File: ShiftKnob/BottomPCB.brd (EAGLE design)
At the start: 38.1 x 38 mm, 38 parts, among them IC2 UA78M05DCY, J1 AVR_SPI_PRG_6PTH, Q1 16MHz, Q2 MOSFET-NCHANNELSMD, Q3 MOSFET-PCHANNELSMD, Q4 MOSFET-NCHANNELSMD, Q5 MOSFET-NCHANNELSMD, Q6 MOSFET-NCHANNELSMD, U1 ATMEGA328, U3 FT232RL-BASICSSOP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

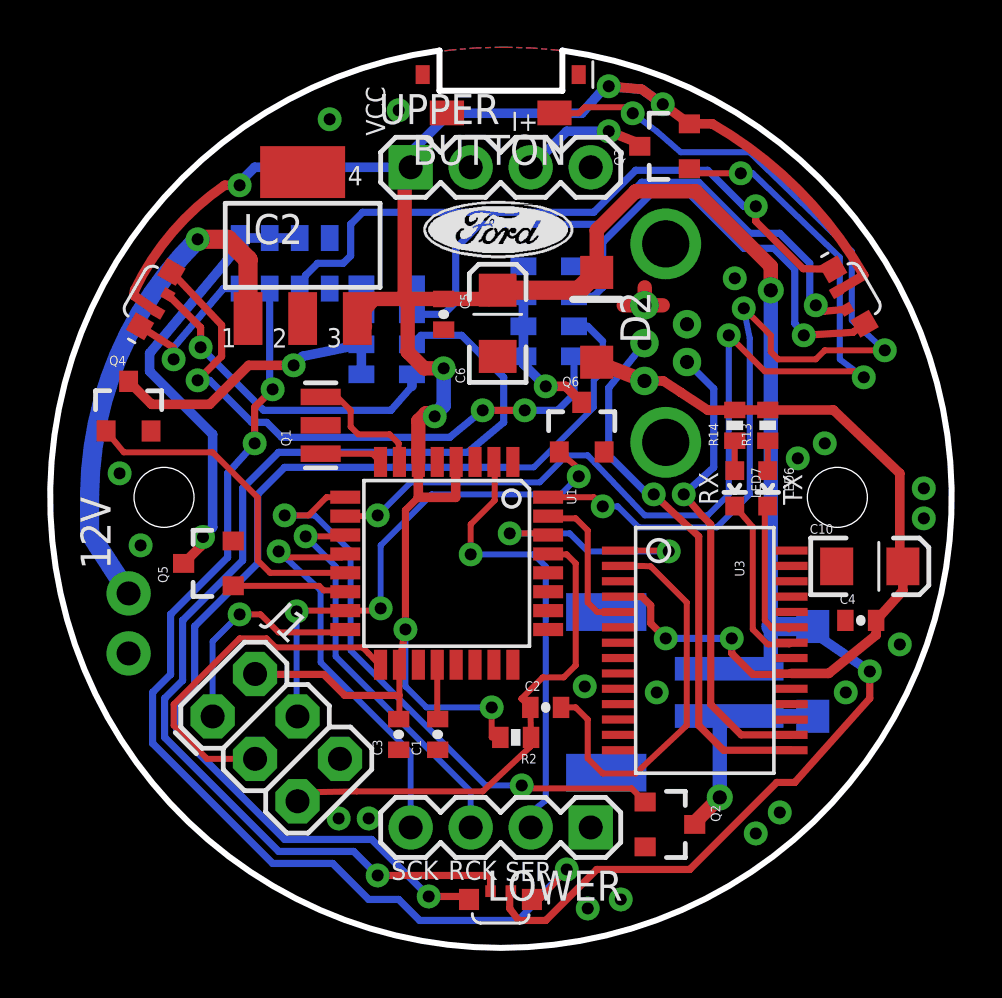
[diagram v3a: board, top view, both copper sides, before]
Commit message: fix board layout to match OSH Park DRU check. regenerate gerber files including the new .GKO outline file needed for OSH.
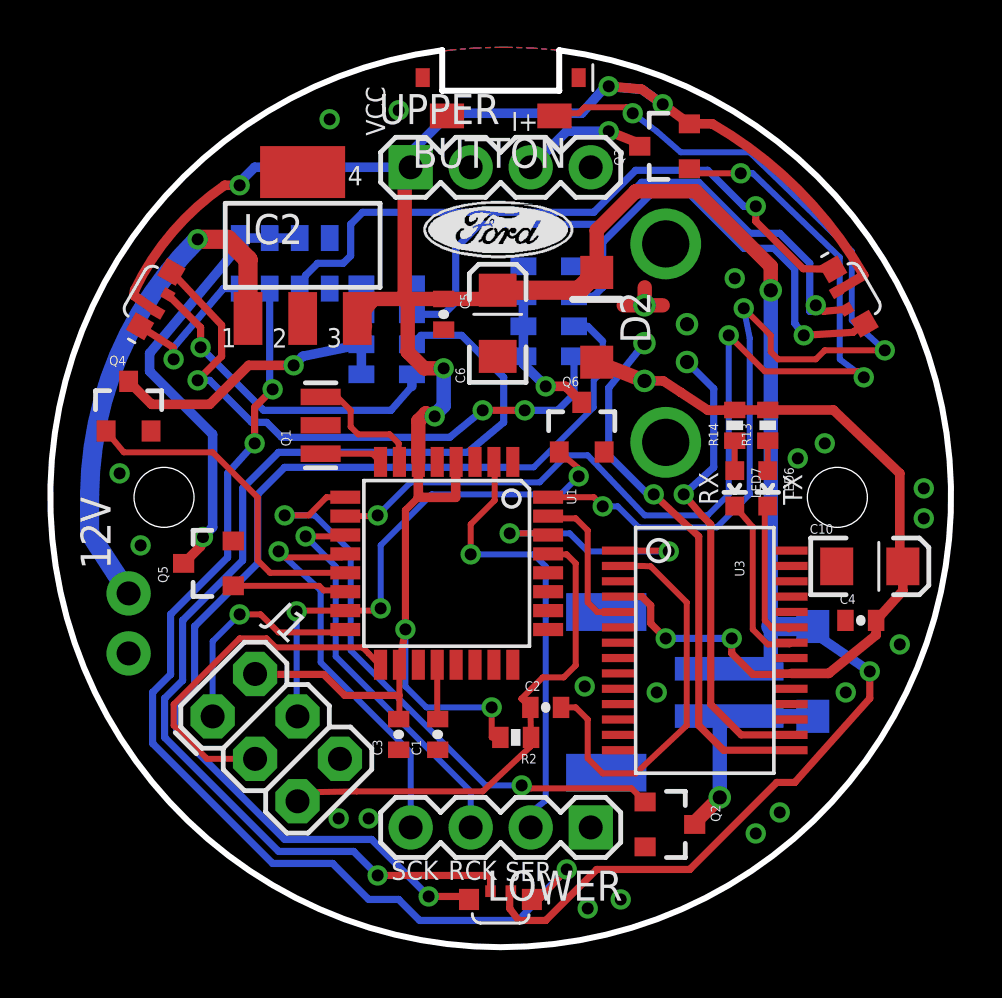
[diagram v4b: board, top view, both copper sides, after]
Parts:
- moved BUTTON 0.13 mm to (21.6, 40.3)
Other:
- outline, holes or cut-outs redrawn
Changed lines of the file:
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@@
 <setting verticaltext="up"/>
 </settings>
-<grid distance="0.005" unitdist="inch" unit="inch" style="lines" multiple="1" display="yes" altdistance="0.025" altunitdist="inch" altunit="inch"/>
+<grid distance="0.0025" unitdist="inch" unit="inch" style="lines" multiple="1" display="yes" altdistance="0.025" altunitdist="inch" altunit="inch"/>
 <layers>
 <layer number="1" name="Top" color="4" fill="1" visible="yes" active="yes"/>
@@
 <circle x="35.8394" y="21.59" radius="2.84988125" width="0.127" layer="49"/>
 <circle x="7.3406" y="21.59" radius="2.84988125" width="0.127" layer="49"/>
-<wire x1="19" y1="40.5" x2="19" y2="38.8" width="0.254" layer="20"/>
-<wire x1="19" y1="38.8" x2="24.2" y2="38.8" width="0.254" layer="20"/>
-<wire x1="24.2" y1="38.8" x2="24.2" y2="40.5" width="0.254" layer="20"/>
-<wire x1="19" y1="40.5" x2="24.2" y2="40.5" width="0.254" layer="20" curve="344.334409"/>
+<wire x1="19.127" y1="38.8" x2="24.073" y2="38.8" width="0.254" layer="20"/>
+<wire x1="19.1135" y1="40.513" x2="24.0665" y2="40.513" width="0.254" layer="20" curve="345.07"/>
 <rectangle x1="21.1861" y1="31.7017" x2="21.7957" y2="31.7271" layer="21"/>
 <rectangle x1="20.7797" y1="31.7271" x2="22.1767" y2="31.7525" layer="21"/>
@@
 <text x="27.3406" y="17.8968" size="1.778" layer="22" rot="MR0">v02</text>
 <dimension x1="2.54" y1="21.59" x2="40.64" y2="21.59" x3="21.59" y3="46.482" layer="48"/>
+<wire x1="19.1135" y1="38.7985" x2="19.1135" y2="40.513" width="0.254" layer="20"/>
+<wire x1="24.0665" y1="38.7985" x2="24.0665" y2="40.513" width="0.254" layer="20"/>
 </plain>
 <attributes>
@@
 </class>
 </classes>
-<designrules name="SparkFun">
-<description language="en">&lt;b&gt;EAGLE Design Rules&lt;/b&gt;
+<designrules name="LaenPCBOrder">
+<description language="de">&lt;b&gt;EAGLE Design Rules&lt;/b&gt;
 &lt;p&gt;
-The default Design Rules have been set to cover
-a wide range of applications. Your particular design
-may have different requirements, so please make the
-necessary adjustments and save your customized
-design rules under a new name.</description>
+Die Standard-Design-Rules sind so gewählt, dass sie für
+die meisten Anwendungen passen. Sollte ihre Platine
+besondere Anforderungen haben, treffen Sie die erforderlichen
+Einstellungen hier und speichern die Design Rules unter
+einem neuen Namen ab.</description>
+<description language="en">&lt;b&gt;Laen's PCB Order Design Rules&lt;/b&gt;
+&lt;p&gt;
+Please make sure your boards conform to these design rules.</description>
 <param name="layerSetup" value="(1*16)"/>
-<param name="mtCopper" value="0.035mm 0.035mm 0.035mm 0.035mm 0.035mm 0.035mm 0.035mm 0.035mm 0.035mm 0.035mm 0.035mm 0.035mm 0.035mm 0.035mm 0.035mm 0.035mm"/>
-<param name="mtIsolate" value="1.5mm 0.15mm 0.2mm 0.15mm 0.2mm 0.15mm 0.2mm 0.15mm 0.2mm 0.15mm 0.2mm 0.15mm 0.2mm 0.15mm 0.2mm"/>
-<param name="mdWireWire" value="8mil"/>
-<param name="mdWirePad" value="8mil"/>
-<param name="mdWireVia" value="8mil"/>
-<param name="mdPadPad" value="8mil"/>
-<param name="mdPadVia" value="8mil"/>
-<param name="mdViaVia" value="8mil"/>
-<param name="mdSmdPad" value="8mil"/>
-<param name="mdSmdVia" value="8mil"/>
-<param name="mdSmdSmd" value="8mil"/>
+<param name="mtCopper" value="0.0356mm 0.0356mm 0.0356mm 0.0356mm 0.0356mm 0.0356mm 0.0356mm 0.0356mm 0.0356mm 0.0356mm 0.0356mm 0.0356mm 0.0356mm 0.0356mm 0.0356mm 0.0356mm"/>
+<param name="mtIsolate" value="1.5011mm 0.1499mm 0.2007mm 0.1499mm 0.2007mm 0.1499mm 0.2007mm 0.1499mm 0.2007mm 0.1499mm 0.2007mm 0.1499mm 0.2007mm 0.1499mm 0.2007mm"/>
+<param name="mdWireWire" value="6mil"/>
+<param name="mdWirePad" value="6mil"/>
+<param name="mdWireVia" value="6mil"/>
+<param name="mdPadPad" value="6mil"/>
+<param name="mdPadVia" value="6mil"/>
+<param name="mdViaVia" value="6mil"/>
+<param name="mdSmdPad" value="6mil"/>
+<param name="mdSmdVia" value="6mil"/>
+<param name="mdSmdSmd" value="6mil"/>
 <param name="mdViaViaSameLayer" value="8mil"/>
 <param name="mnLayersViaInSmd" value="2"/>
-<param name="mdCopperDimension" value="10mil"/>
-<param name="mdDrill" value="8mil"/>
+<param name="mdCopperDimension" value="15mil"/>
+<param name="mdDrill" value="6mil"/>
 <param name="mdSmdStop" value="0mil"/>
-<param name="msWidth" value="8mil"/>
-<param name="msDrill" value="20mil"/>
-<param name="msMicroVia" value="9.99mm"/>
+<param name="msWidth" value="6mil"/>
+<param name="msDrill" value="13mil"/>
+<param name="msMicroVia" value="13mil"/>
 <param name="msBlindViaRatio" value="0.5"/>
 <param name="rvPadTop" value="0.25"/>
@@
 <param name="rvMicroViaOuter" value="0.25"/>
 <param name="rvMicroViaInner" value="0.25"/>
-<param name="rlMinPadTop" value="12mil"/>
+<param name="rlMinPadTop" value="7mil"/>
 <param name="rlMaxPadTop" value="20mil"/>
-<param name="rlMinPadInner" value="10mil"/>
+<param name="rlMinPadInner" value="7mil"/>
 <param name="rlMaxPadInner" value="20mil"/>
-<param name="rlMinPadBottom" value="12mil"/>
+<param name="rlMinPadBottom" value="7mil"/>
 <param name="rlMaxPadBottom" value="20mil"/>
-<param name="rlMinViaOuter" value="10mil"/>
+<param name="rlMinViaOuter" value="7mil"/>
 <param name="rlMaxViaOuter" value="20mil"/>
-<param name="rlMinViaInner" value="10mil"/>
+<param name="rlMinViaInner" value="7mil"/>
 <param name="rlMaxViaInner" value="20mil"/>
 <param name="rlMinMicroViaOuter" value="4mil"/>
@@
 <param name="mlMinCreamFrame" value="0mil"/>
 <param name="mlMaxCreamFrame" value="0mil"/>
-<param name="mlViaStopLimit" value="25mil"/>
+<param name="mlViaStopLimit" value="0mil"/>
 <param name="srRoundness" value="0"/>
 <param name="srMinRoundness" value="0mil"/>
@@
 </element>
 <element name="C4" library="SparkFun" package="0402-CAP" value="0.1uF" x="36.83" y="16.383"/>
-<element name="BUTTON" library="FORD_frames" package="BUTTON_EDGE" value="BUTTON_EDGE" x="21.59" y="40.432" rot="R180"/>
+<element name="BUTTON" library="FORD_frames" package="BUTTON_EDGE" value="BUTTON_EDGE" x="21.59" y="40.305" rot="R180"/>
 <element name="UPPER" library="SparkFun-Connectors" package="1X04" value="" x="17.78" y="35.56"/>
 <element name="LOWER" library="SparkFun-Connectors" package="1X04" value="" x="25.4" y="7.62" rot="R180"/>
@@
 <wire x1="26.543" y1="21.209" x2="27.432" y2="20.32" width="0.254" layer="16"/>
 <wire x1="27.432" y1="20.32" x2="30.734" y2="20.32" width="0.254" layer="16"/>
-<wire x1="23.865" y1="37.862" x2="24.384" y2="37.846" width="0.254" layer="1"/>
+<wire x1="23.865" y1="37.735" x2="24.384" y2="37.846" width="0.254" layer="1"/>
 <via x="27.178" y="37.846" extent="1-16" drill="0.508"/>
 <wire x1="27.178" y1="37.846" x2="28.194" y2="37.084" width="0.254" layer="16"/>
